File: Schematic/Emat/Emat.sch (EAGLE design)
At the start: 42 parts, among them J1 PIN1-2, J2 PIN1-2, J3 PIN1-2, J4 PIN1-2, J5 PIN1-2, J8 PIN1-2, J9 PIN1-2, Q2 STP13NM60NTO220BVH, U1 UCC27324D, X2 22-23-2021, X3 22-23-2021, X4 22-23-2021, X5 22-23-2021, X6 22-23-2021

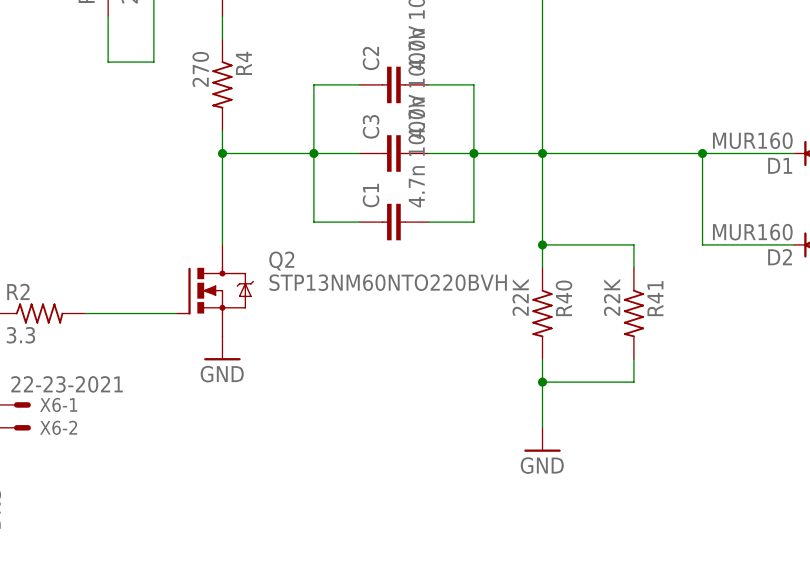
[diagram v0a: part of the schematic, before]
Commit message: Modify board to fit to pcb.
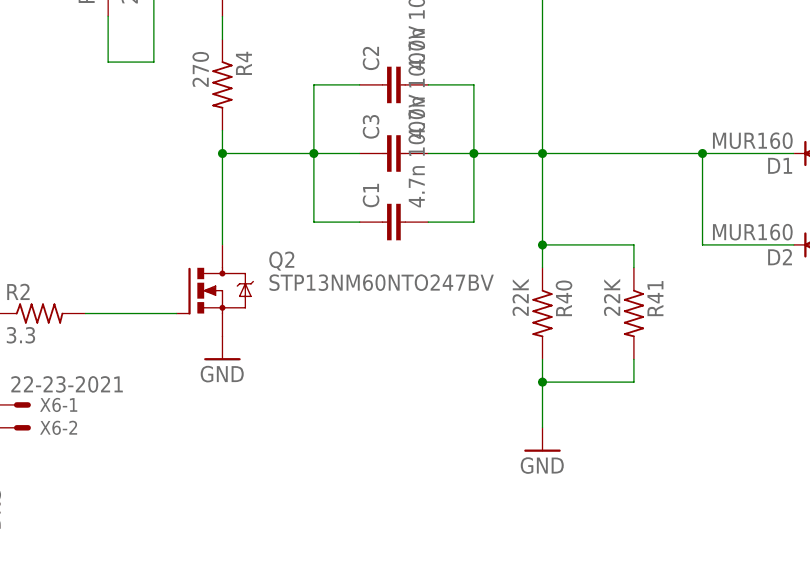
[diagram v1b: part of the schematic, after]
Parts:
- Q2: value STP13NM60NTO220BVH -> STP13NM60NTO247BV; device transistor-power:STP13NM60NTO220BVH -> transistor-power:STP13NM60NTO247BV
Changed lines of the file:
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@@
 <grid distance="0.1" unitdist="inch" unit="inch" style="lines" multiple="1" display="no" altdistance="0.01" altunitdist="inch" altunit="inch"/>
 <layers>
-<layer number="1" name="Top" color="4" fill="1" visible="no" active="no"/>
-<layer number="16" name="Bottom" color="1" fill="1" visible="no" active="no"/>
-<layer number="17" name="Pads" color="2" fill="1" visible="no" active="no"/>
-<layer number="18" name="Vias" color="2" fill="1" visible="no" active="no"/>
-<layer number="19" name="Unrouted" color="6" fill="1" visible="no" active="no"/>
-<layer number="20" name="Dimension" color="15" fill="1" visible="no" active="no"/>
-<layer number="21" name="tPlace" color="7" fill="1" visible="no" active="no"/>
-<layer number="22" name="bPlace" color="7" fill="1" visible="no" active="no"/>
-<layer number="23" name="tOrigins" color="15" fill="1" visible="no" active="no"/>
-<layer number="24" name="bOrigins" color="15" fill="1" visible="no" active="no"/>
-<layer number="25" name="tNames" color="7" fill="1" visible="no" active="no"/>
-<layer number="26" name="bNames" color="7" fill="1" visible="no" active="no"/>
-<layer number="27" name="tValues" color="7" fill="1" visible="no" active="no"/>
-<layer number="28" name="bValues" color="7" fill="1" visible="no" active="no"/>
+<layer number="1" name="Top" color="4" fill="1" visible="yes" active="no"/>
+<layer number="16" name="Bottom" color="1" fill="1" visible="yes" active="no"/>
+<layer number="17" name="Pads" color="2" fill="1" visible="yes" active="no"/>
+<layer number="18" name="Vias" color="2" fill="1" visible="yes" active="no"/>
+<layer number="19" name="Unrouted" color="6" fill="1" visible="yes" active="no"/>
+<layer number="20" name="Dimension" color="15" fill="1" visible="yes" active="no"/>
+<layer number="21" name="tPlace" color="7" fill="1" visible="yes" active="no"/>
+<layer number="22" name="bPlace" color="7" fill="1" visible="yes" active="no"/>
+<layer number="23" name="tOrigins" color="15" fill="1" visible="yes" active="no"/>
+<layer number="24" name="bOrigins" color="15" fill="1" visible="yes" active="no"/>
+<layer number="25" name="tNames" color="7" fill="1" visible="yes" active="no"/>
+<layer number="26" name="bNames" color="7" fill="1" visible="yes" active="no"/>
+<layer number="27" name="tValues" color="7" fill="1" visible="yes" active="no"/>
+<layer number="28" name="bValues" color="7" fill="1" visible="yes" active="no"/>
 <layer number="29" name="tStop" color="7" fill="3" visible="no" active="no"/>
 <layer number="30" name="bStop" color="7" fill="6" visible="no" active="no"/>
@@
 <layer number="35" name="tGlue" color="7" fill="4" visible="no" active="no"/>
 <layer number="36" name="bGlue" color="7" fill="5" visible="no" active="no"/>
-<layer number="37" name="tTest" color="7" fill="1" visible="no" active="no"/>
-<layer number="38" name="bTest" color="7" fill="1" visible="no" active="no"/>
+<layer number="37" name="tTest" color="7" fill="1" visible="yes" active="no"/>
+<layer number="38" name="bTest" color="7" fill="1" visible="yes" active="no"/>
 <layer number="39" name="tKeepout" color="4" fill="11" visible="no" active="no"/>
 <layer number="40" name="bKeepout" color="1" fill="11" visible="no" active="no"/>
@@
 <layer number="44" name="Drills" color="7" fill="1" visible="no" active="no"/>
 <layer number="45" name="Holes" color="7" fill="1" visible="no" active="no"/>
-<layer number="46" name="Milling" color="3" fill="1" visible="no" active="no"/>
-<layer number="47" name="Measures" color="7" fill="1" visible="no" active="no"/>
-<layer number="48" name="Document" color="7" fill="1" visible="no" active="no"/>
-<layer number="49" name="Reference" color="7" fill="1" visible="no" active="no"/>
-<layer number="51" name="tDocu" color="7" fill="1" visible="no" active="no"/>
-<layer number="52" name="bDocu" color="7" fill="1" visible="no" active="no"/>
+<layer number="46" name="Milling" color="3" fill="1" visible="yes" active="no"/>
+<layer number="47" name="Measures" color="7" fill="1" visible="yes" active="no"/>
+<layer number="48" name="Document" color="7" fill="1" visible="yes" active="no"/>
+<layer number="49" name="Reference" color="7" fill="1" visible="yes" active="no"/>
+<layer number="51" name="tDocu" color="7" fill="1" visible="yes" active="no"/>
+<layer number="52" name="bDocu" color="7" fill="1" visible="yes" active="no"/>
 <layer number="90" name="Modules" color="5" fill="1" visible="yes" active="yes"/>
 <layer number="91" name="Nets" color="2" fill="1" visible="yes" active="yes"/>
@@
 <part name="R1" library="rcl" deviceset="R-US_" device="R1206" value="10K"/>
 <part name="R2" library="rcl" deviceset="R-US_" device="R1206" value="3.3"/>
-<part name="Q2" library="transistor-power" deviceset="STP13NM60N" device="TO220BVH" value="STP13NM60NTO220BVH"/>
+<part name="Q2" library="transistor-power" deviceset="STP13NM60N" device="TO247BV" value="STP13NM60NTO247BV"/>
 <part name="R40" library="rcl" deviceset="R-US_" device="R2512" value="22K"/>
 <part name="R41" library="rcl" deviceset="R-US_" device="R2512" value="22K"/>

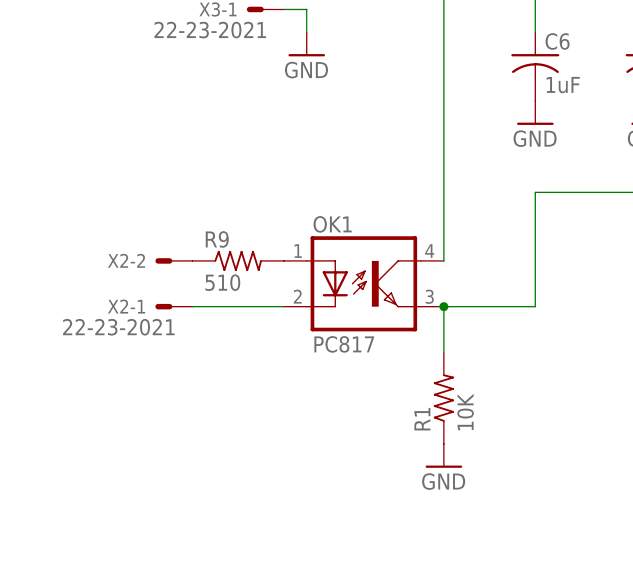
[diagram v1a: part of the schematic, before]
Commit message: Fix schematic. 1.5KE300 added.
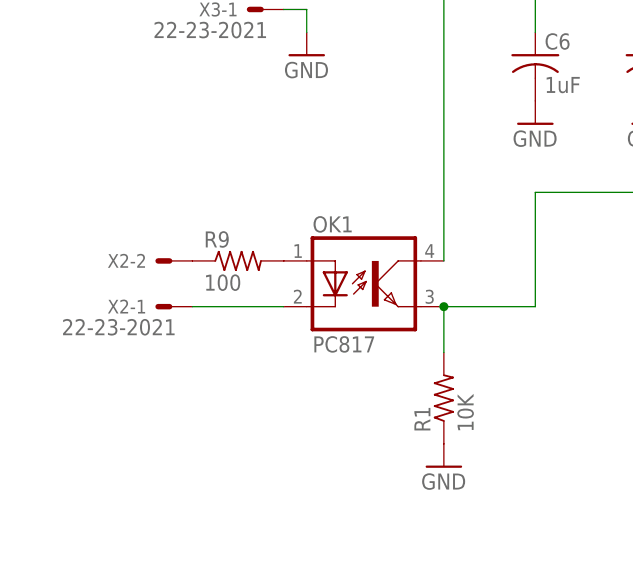
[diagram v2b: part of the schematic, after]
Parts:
- R9: value 510 -> 100
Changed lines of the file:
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@@
 <grid distance="0.1" unitdist="inch" unit="inch" style="lines" multiple="1" display="no" altdistance="0.01" altunitdist="inch" altunit="inch"/>
 <layers>
-<layer number="1" name="Top" color="4" fill="1" visible="yes" active="no"/>
-<layer number="16" name="Bottom" color="1" fill="1" visible="yes" active="no"/>
-<layer number="17" name="Pads" color="2" fill="1" visible="yes" active="no"/>
-<layer number="18" name="Vias" color="2" fill="1" visible="yes" active="no"/>
-<layer number="19" name="Unrouted" color="6" fill="1" visible="yes" active="no"/>
-<layer number="20" name="Dimension" color="15" fill="1" visible="yes" active="no"/>
-<layer number="21" name="tPlace" color="7" fill="1" visible="yes" active="no"/>
-<layer number="22" name="bPlace" color="7" fill="1" visible="yes" active="no"/>
-<layer number="23" name="tOrigins" color="15" fill="1" visible="yes" active="no"/>
-<layer number="24" name="bOrigins" color="15" fill="1" visible="yes" active="no"/>
-<layer number="25" name="tNames" color="7" fill="1" visible="yes" active="no"/>
-<layer number="26" name="bNames" color="7" fill="1" visible="yes" active="no"/>
-<layer number="27" name="tValues" color="7" fill="1" visible="yes" active="no"/>
-<layer number="28" name="bValues" color="7" fill="1" visible="yes" active="no"/>
+<layer number="1" name="Top" color="4" fill="1" visible="no" active="no"/>
+<layer number="16" name="Bottom" color="1" fill="1" visible="no" active="no"/>
+<layer number="17" name="Pads" color="2" fill="1" visible="no" active="no"/>
+<layer number="18" name="Vias" color="2" fill="1" visible="no" active="no"/>
+<layer number="19" name="Unrouted" color="6" fill="1" visible="no" active="no"/>
+<layer number="20" name="Dimension" color="15" fill="1" visible="no" active="no"/>
+<layer number="21" name="tPlace" color="7" fill="1" visible="no" active="no"/>
+<layer number="22" name="bPlace" color="7" fill="1" visible="no" active="no"/>
+<layer number="23" name="tOrigins" color="15" fill="1" visible="no" active="no"/>
+<layer number="24" name="bOrigins" color="15" fill="1" visible="no" active="no"/>
+<layer number="25" name="tNames" color="7" fill="1" visible="no" active="no"/>
+<layer number="26" name="bNames" color="7" fill="1" visible="no" active="no"/>
+<layer number="27" name="tValues" color="7" fill="1" visible="no" active="no"/>
+<layer number="28" name="bValues" color="7" fill="1" visible="no" active="no"/>
 <layer number="29" name="tStop" color="7" fill="3" visible="no" active="no"/>
 <layer number="30" name="bStop" color="7" fill="6" visible="no" active="no"/>
@@
 <layer number="35" name="tGlue" color="7" fill="4" visible="no" active="no"/>
 <layer number="36" name="bGlue" color="7" fill="5" visible="no" active="no"/>
-<layer number="37" name="tTest" color="7" fill="1" visible="yes" active="no"/>
-<layer number="38" name="bTest" color="7" fill="1" visible="yes" active="no"/>
+<layer number="37" name="tTest" color="7" fill="1" visible="no" active="no"/>
+<layer number="38" name="bTest" color="7" fill="1" visible="no" active="no"/>
 <layer number="39" name="tKeepout" color="4" fill="11" visible="no" active="no"/>
 <layer number="40" name="bKeepout" color="1" fill="11" visible="no" active="no"/>
@@
 <layer number="44" name="Drills" color="7" fill="1" visible="no" active="no"/>
 <layer number="45" name="Holes" color="7" fill="1" visible="no" active="no"/>
-<layer number="46" name="Milling" color="3" fill="1" visible="yes" active="no"/>
-<layer number="47" name="Measures" color="7" fill="1" visible="yes" active="no"/>
-<layer number="48" name="Document" color="7" fill="1" visible="yes" active="no"/>
-<layer number="49" name="Reference" color="7" fill="1" visible="yes" active="no"/>
-<layer number="51" name="tDocu" color="7" fill="1" visible="yes" active="no"/>
-<layer number="52" name="bDocu" color="7" fill="1" visible="yes" active="no"/>
+<layer number="46" name="Milling" color="3" fill="1" visible="no" active="no"/>
+<layer number="47" name="Measures" color="7" fill="1" visible="no" active="no"/>
+<layer number="48" name="Document" color="7" fill="1" visible="no" active="no"/>
+<layer number="49" name="Reference" color="7" fill="1" visible="no" active="no"/>
+<layer number="51" name="tDocu" color="7" fill="1" visible="no" active="no"/>
+<layer number="52" name="bDocu" color="7" fill="1" visible="no" active="no"/>
 <layer number="90" name="Modules" color="5" fill="1" visible="yes" active="yes"/>
 <layer number="91" name="Nets" color="2" fill="1" visible="yes" active="yes"/>
@@
 <part name="OK1" library="optocoupler" deviceset="PC817" device=""/>
 <part name="X2" library="con-molex" deviceset="22-23-2021" device=""/>
-<part name="R9" library="rcl" deviceset="R-US_" device="R1206" value="510"/>
+<part name="R9" library="rcl" deviceset="R-US_" device="R1206" value="100"/>
 <part name="GND15" library="supply1" deviceset="GND" device=""/>
 <part name="X3" library="con-molex" deviceset="22-23-2021" device=""/>
